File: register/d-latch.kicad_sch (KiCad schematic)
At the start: 0 parts

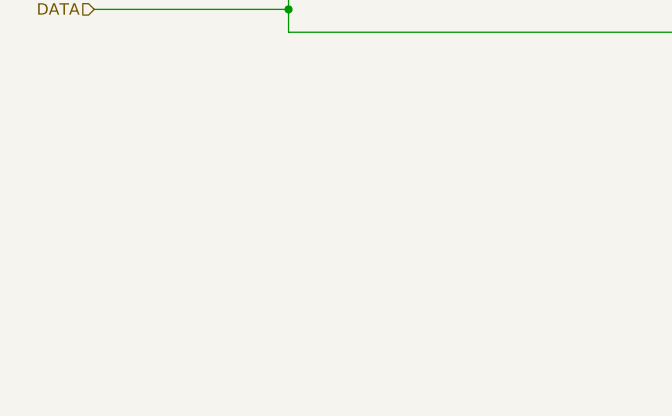
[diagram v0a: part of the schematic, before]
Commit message: Use IC circuits in adder circuit
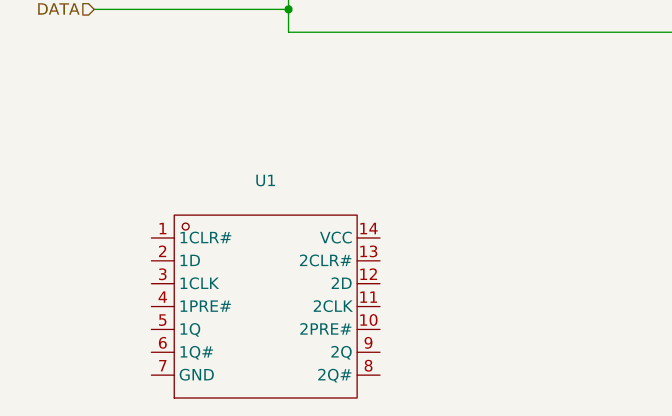
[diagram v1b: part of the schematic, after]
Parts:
- added U1: ~, SN74HC74N:PDIP-14_L19.3-W6.4-P2.54-LS7.6-BL, symbol SN74HC74N:SN74HC74N
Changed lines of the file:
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@@
+		)
+	)
+	(symbol
+		(lib_id "SN74HC74N:SN74HC74N")
+		(at 45.72 110.49 0)
+		(unit 1)
+		(exclude_from_sim no)
+		(in_bom yes)
+		(on_board yes)
+		(dnp no)
+		(fields_autoplaced yes)
+		(property "Reference" "U1"
+			(at 45.72 96.52 0)
+			(effects
+				(font
+					(size 1.27 1.27)
+				)
+			)
+		)
+		(property "Value" "~"
+			(at 45.72 99.06 0)
+			(effects
+				(font
+					(size 1.27 1.27)
+				)
+			)
+		)
+		(property "Footprint" "SN74HC74N:PDIP-14_L19.3-W6.4-P2.54-LS7.6-BL"
+			(at 45.72 110.49 0)
+			(effects
+				(font
+					(size 1.27 1.27)
+				)
+				(hide yes)
+			)
+		)
+		(property "Datasheet" "https://www.ti.com/cn/lit/gpn/sn74hc74"
+			(at 45.72 110.49 0)
+			(effects
+				(font
+					(size 1.27 1.27)
+				)
+				(hide yes)
+			)
+		)
+		(property "Description" "Type:D-Type Trigger Type:Rising Edge Supply Voltage:2V~6V Supply Voltage:2V~6V Clock Frequency:60MHz Function:Positioning and resetting Number of Elements:2 Number of Bits per Element:1 Output Type:Complementary Type Maximum Propagation Delay:30ns@6V,50pF"
+			(at 45.72 110.49 0)
+			(effects
+				(font
+					(size 1.27 1.27)
+				)
+				(hide yes)
+			)
+		)
+		(property "Manufacturer Part" "SN74HC74N"
+			(at 45.72 110.49 0)
+			(effects
+				(font
+					(size 1.27 1.27)
+				)
+				(hide yes)
+			)
+		)
+		(property "Manufacturer" "TI(德州仪器)"
+			(at 45.72 110.49 0)
+			(effects
+				(font
+					(size 1.27 1.27)
+				)
+				(hide yes)
+			)
+		)
+		(property "Supplier Part" "C2895"
+			(at 45.72 110.49 0)
+			(effects
+				(font
+					(size 1.27 1.27)
+				)
+				(hide yes)
+			)
+		)
+		(property "Supplier" "LCSC"
+			(at 45.72 110.49 0)
+			(effects
+				(font
+					(size 1.27 1.27)
+				)
+				(hide yes)
+			)
+		)
+		(property "LCSC Part Name" "SN74HC74N"
+			(at 45.72 110.49 0)
+			(effects
+				(font
+					(size 1.27 1.27)
+				)
+				(hide yes)
+			)
+		)
+		(pin "13"
+		)
+		(pin "9"
+		)
+		(pin "11"
+		)
+		(pin "5"
+		)
+		(pin "4"
+		)
+		(pin "8"
+		)
+		(pin "2"
+		)
+		(pin "12"
+		)
+		(pin "3"
+		)
+		(pin "6"
+		)
+		(pin "7"
+		)
+		(pin "14"
+		)
+		(pin "1"
+		)
+		(pin "10"
+		)
+		(instances
+			(project ""
+				(path "/176ebc34-d92d-46b0-a9f1-4fb76aa55196/1641c1b9-e3d9-452a-a206-0a4a18cb7a68"
+					(reference "U2")
+					(unit 1)
+				)
+				(path "/176ebc34-d92d-46b0-a9f1-4fb76aa55196/2b210005-c9ef-43dd-bd20-4304cf65b93c"
+					(reference "U1")
+					(unit 1)
+				)
+				(path "/176ebc34-d92d-46b0-a9f1-4fb76aa55196/475a755d-c11d-42bc-b5a5-c2bbb617acf6"
+					(reference "U4")
+					(unit 1)
+				)
+				(path "/176ebc34-d92d-46b0-a9f1-4fb76aa55196/510c109f-9f77-4fcd-9065-7421496291db"
+					(reference "U3")
+					(unit 1)
+				)
+			)
 		)
 	)
